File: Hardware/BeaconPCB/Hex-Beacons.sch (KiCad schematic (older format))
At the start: 0 parts

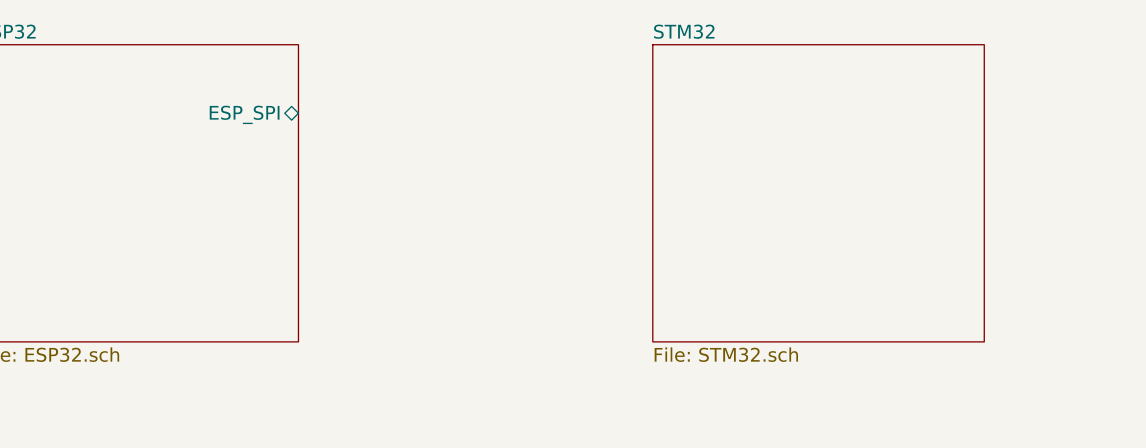
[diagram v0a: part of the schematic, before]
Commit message: Base STM32 circuit schematic done
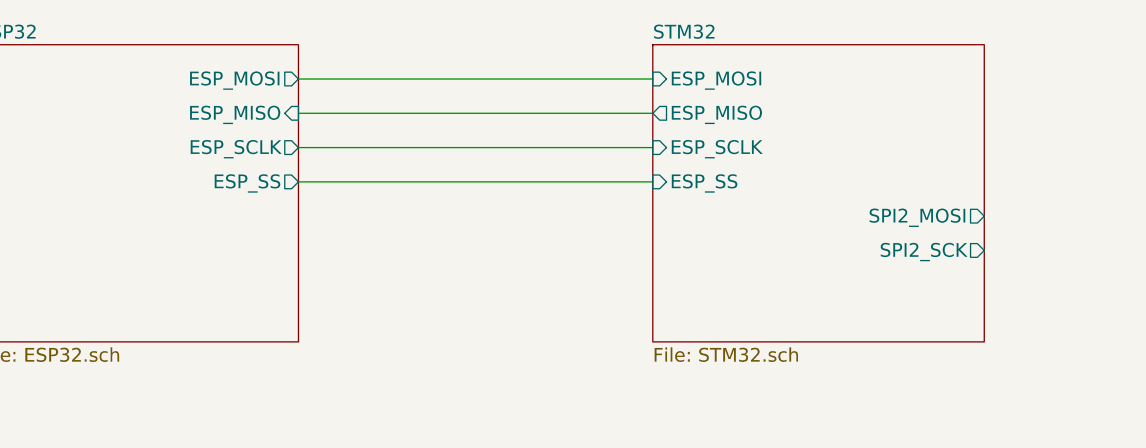
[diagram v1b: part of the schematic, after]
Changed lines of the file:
@@
 F0 "ESP32" 60
 F1 "ESP32.sch" 60
-F2 "ESP_SPI" B R 4400 2600 60
+F2 "ESP_MOSI" O R 4400 2450 60
+F3 "ESP_MISO" I R 4400 2600 60
+F4 "ESP_SCLK" O R 4400 2750 60
+F5 "ESP_SS" O R 4400 2900 60
 $EndSheet
 $Sheet
@@
 F0 "STM32" 60
 F1 "STM32.sch" 60
+F2 "ESP_SS" I L 5950 2900 60
+F3 "ESP_SCLK" I L 5950 2750 60
+F4 "ESP_MISO" O L 5950 2600 60
+F5 "ESP_MOSI" I L 5950 2450 60
+F6 "SPI2_MOSI" O R 7400 3050 60
+F7 "SPI2_SCK" O R 7400 3200 60
 $EndSheet
 $Sheet
@@
 F1 "APA102.sch" 60
 $EndSheet
+Wire Wire Line
+	4400 2450 5950 2450
+Wire Wire Line
+	5950 2600 4400 2600
+Wire Wire Line
+	4400 2750 5950 2750
+Wire Wire Line
+	5950 2900 4400 2900
 $EndSCHEMATC

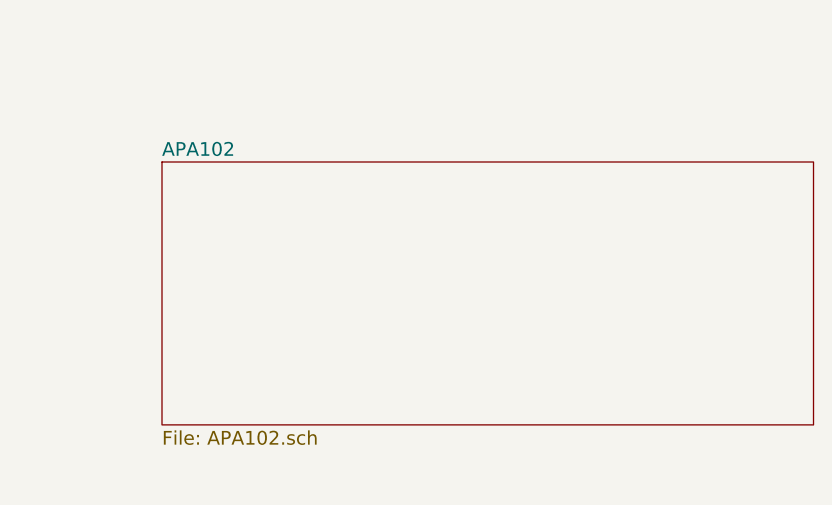
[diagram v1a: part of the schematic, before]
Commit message: Added IO buffers and APA102
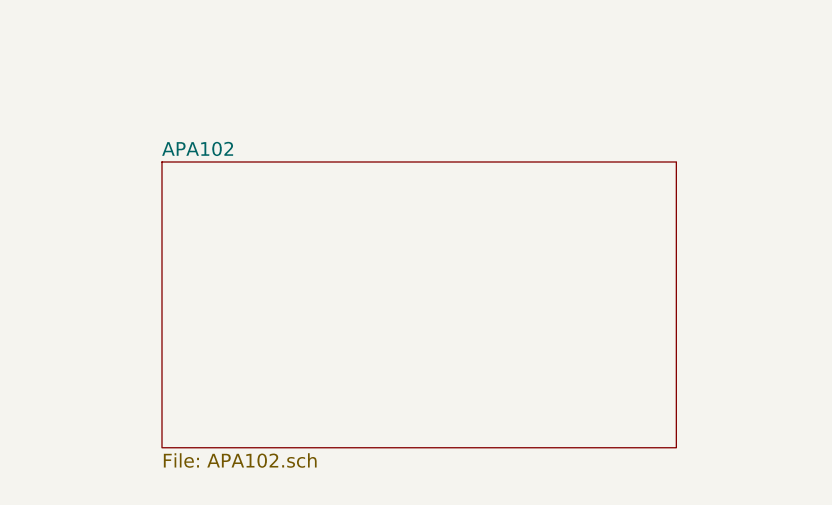
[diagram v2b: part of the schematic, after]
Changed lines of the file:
@@
 LIBS:valves
 LIBS:STM32F042C6T6
+LIBS:crumpschemes
 LIBS:Hex-Beacons-cache
 EELAYER 25 0
@@
 $EndSheet
 $Sheet
-S 7000 4650 2850 1150
+S 7000 4650 2250 1250
 U 59ADAAF7
 F0 "APA102" 60

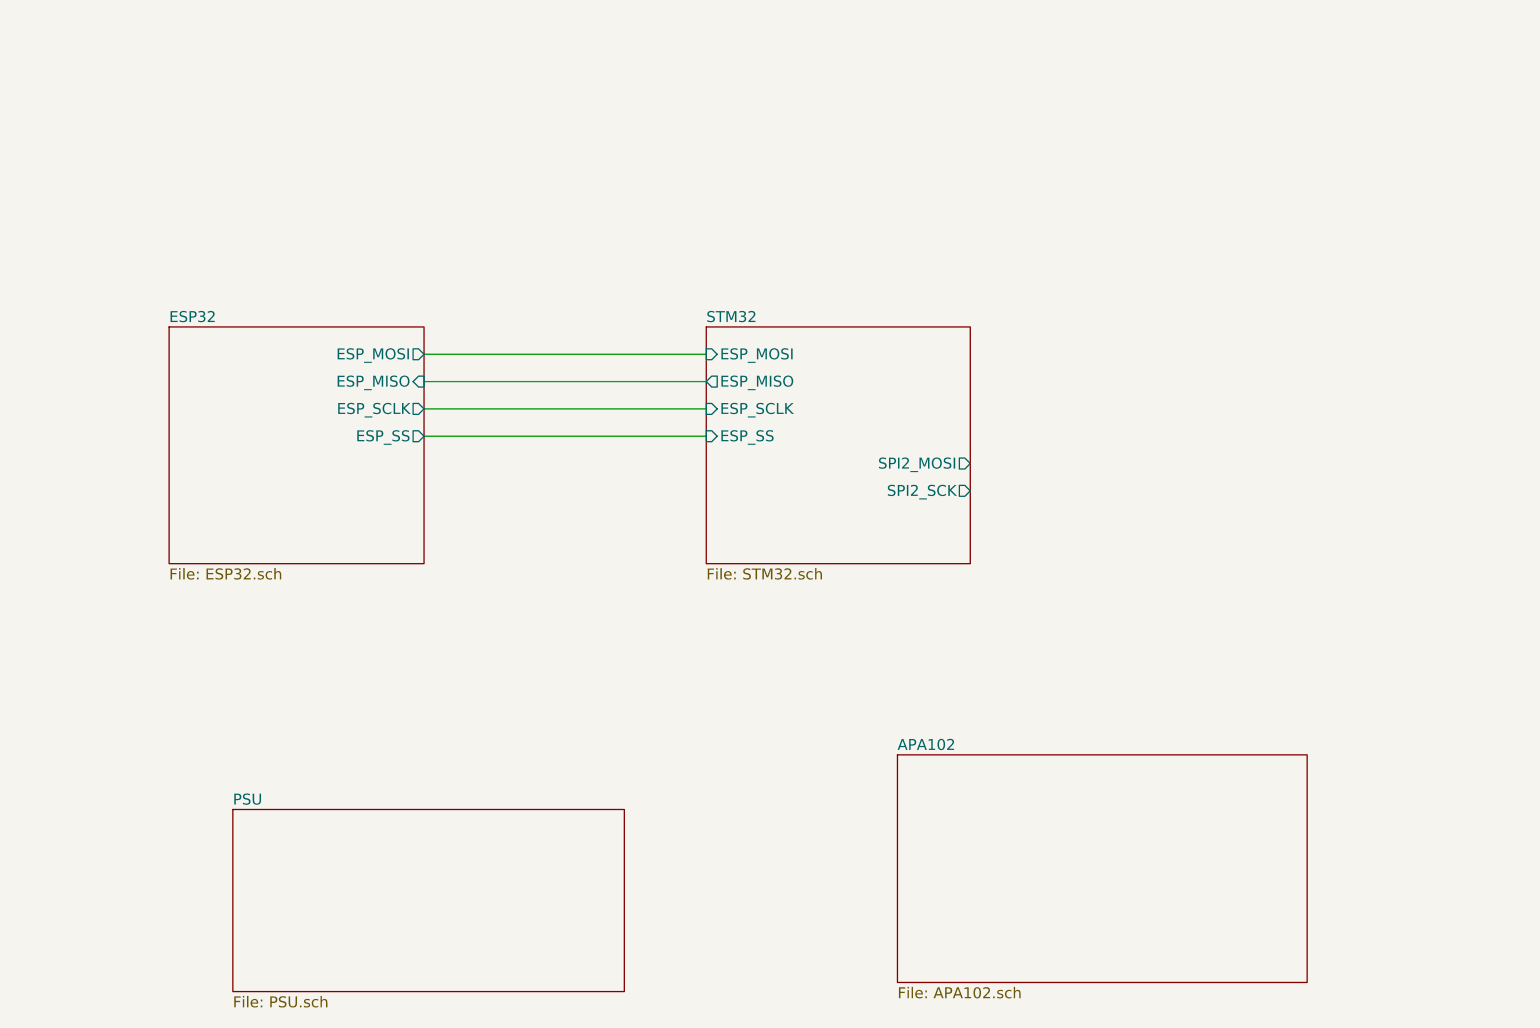
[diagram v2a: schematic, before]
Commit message: Added Connectors Sheet
Started to re-arrange SPI lines
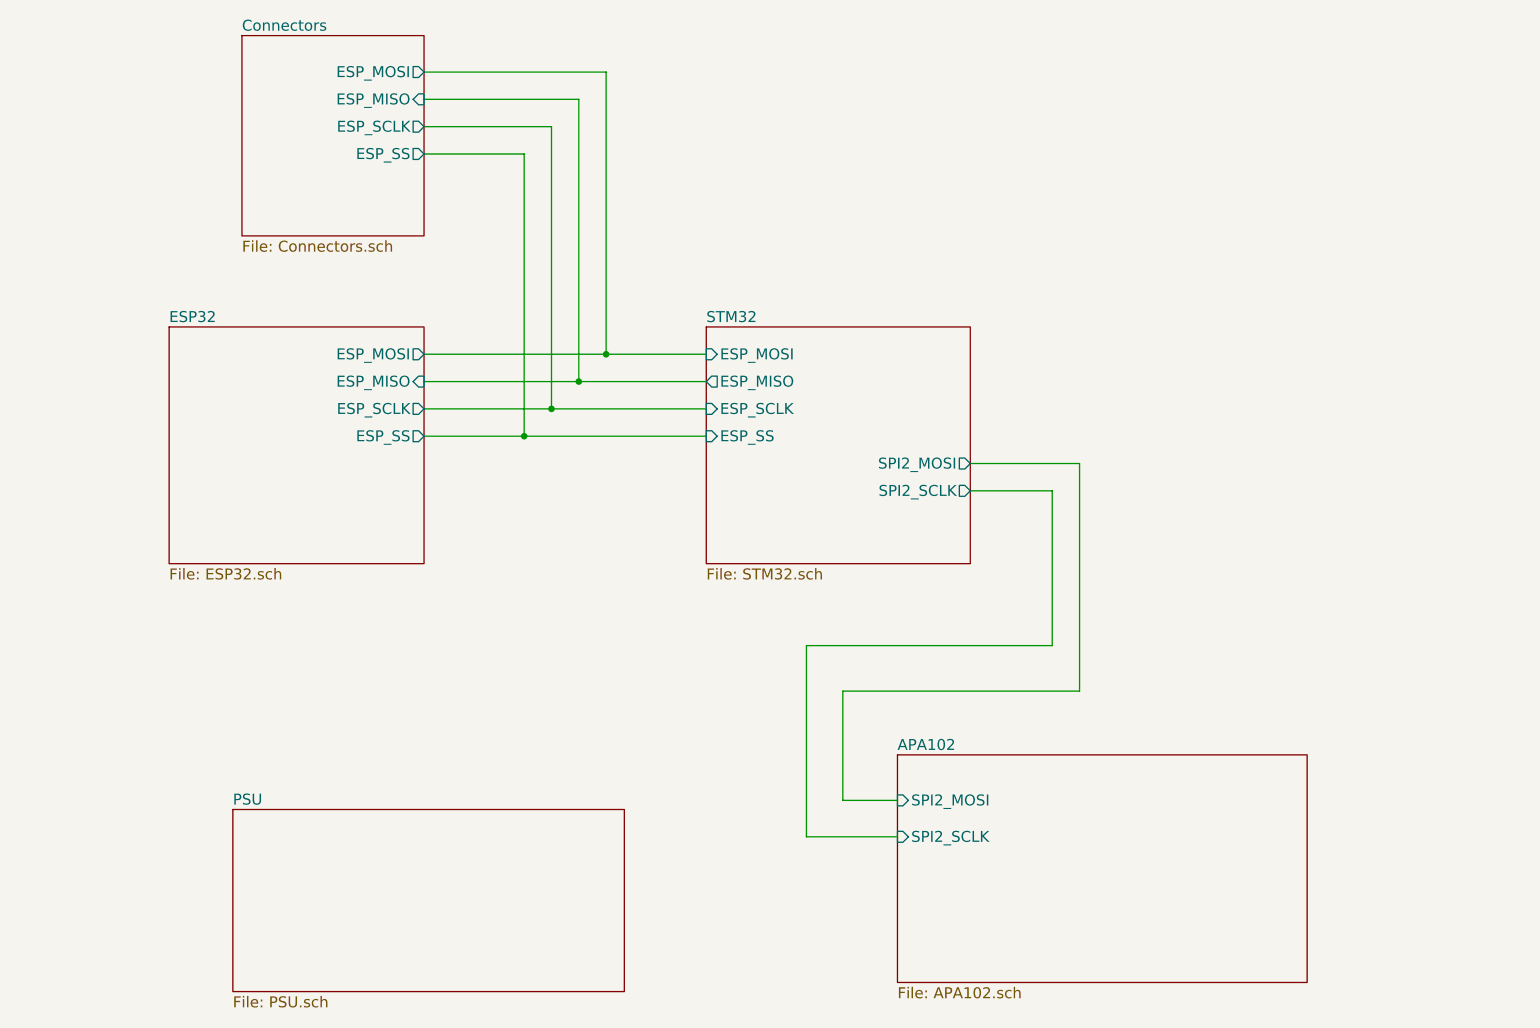
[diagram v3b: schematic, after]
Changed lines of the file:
@@
 $Descr A4 11693 8268
 encoding utf-8
-Sheet 1 5
+Sheet 1 6
 Title ""
 Date ""
@@
 F5 "ESP_MOSI" I L 5950 2450 60
 F6 "SPI2_MOSI" O R 7400 3050 60
-F7 "SPI2_SCK" O R 7400 3200 60
+F7 "SPI2_SCLK" O R 7400 3200 60
 $EndSheet
 $Sheet
@@
 F0 "APA102" 60
 F1 "APA102.sch" 60
+F2 "SPI2_MOSI" I L 7000 4900 60
+F3 "SPI2_SCLK" I L 7000 5100 60
 $EndSheet
 Wire Wire Line
-	4400 2450 5950 2450
+	4400 2450 5400 2450
 Wire Wire Line
-	5950 2600 4400 2600
+	5400 2450 5950 2450
 Wire Wire Line
-	4400 2750 5950 2750
+	5950 2600 5250 2600
 Wire Wire Line
-	5950 2900 4400 2900
+	5250 2600 4400 2600
+Wire Wire Line
+	4400 2750 5100 2750
+Wire Wire Line
+	5100 2750 5950 2750
+Wire Wire Line
+	5950 2900 4950 2900
+Wire Wire Line
+	4950 2900 4400 2900
+$Sheet
+S 3400 700  1000 1100
+U 59B35FE0
+F0 "Connectors" 60
+F1 "Connectors.sch" 60
+F2 "ESP_MOSI" O R 4400 900 60
+F3 "ESP_MISO" I R 4400 1050 60
+F4 "ESP_SCLK" O R 4400 1200 60
+F5 "ESP_SS" O R 4400 1350 60
+$EndSheet
+Wire Wire Line
+	7000 5100 6500 5100
+Wire Wire Line
+	6500 5100 6500 4050
+Wire Wire Line
+	6500 4050 7850 4050
+Wire Wire Line
+	7850 4050 7850 3200
+Wire Wire Line
+	7850 3200 7400 3200
+Wire Wire Line
+	7400 3050 8000 3050
+Wire Wire Line
+	8000 3050 8000 4300
+Wire Wire Line
+	8000 4300 6700 4300
+Wire Wire Line
+	6700 4300 6700 4900
+Wire Wire Line
+	6700 4900 7000 4900
+Wire Wire Line
+	4400 1350 4950 1350
+Wire Wire Line
+	4950 1350 4950 2900
+Connection ~ 4950 2900
+Wire Wire Line
+	4400 1200 5100 1200
+Wire Wire Line
+	5100 1200 5100 2750
+Connection ~ 5100 2750
+Wire Wire Line
+	4400 1050 5250 1050
+Wire Wire Line
+	5250 1050 5250 2600
+Connection ~ 5250 2600
+Wire Wire Line
+	4400 900  5400 900
+Wire Wire Line
+	5400 900  5400 2450
+Connection ~ 5400 2450
 $EndSCHEMATC

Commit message: Minor schematic adjustments
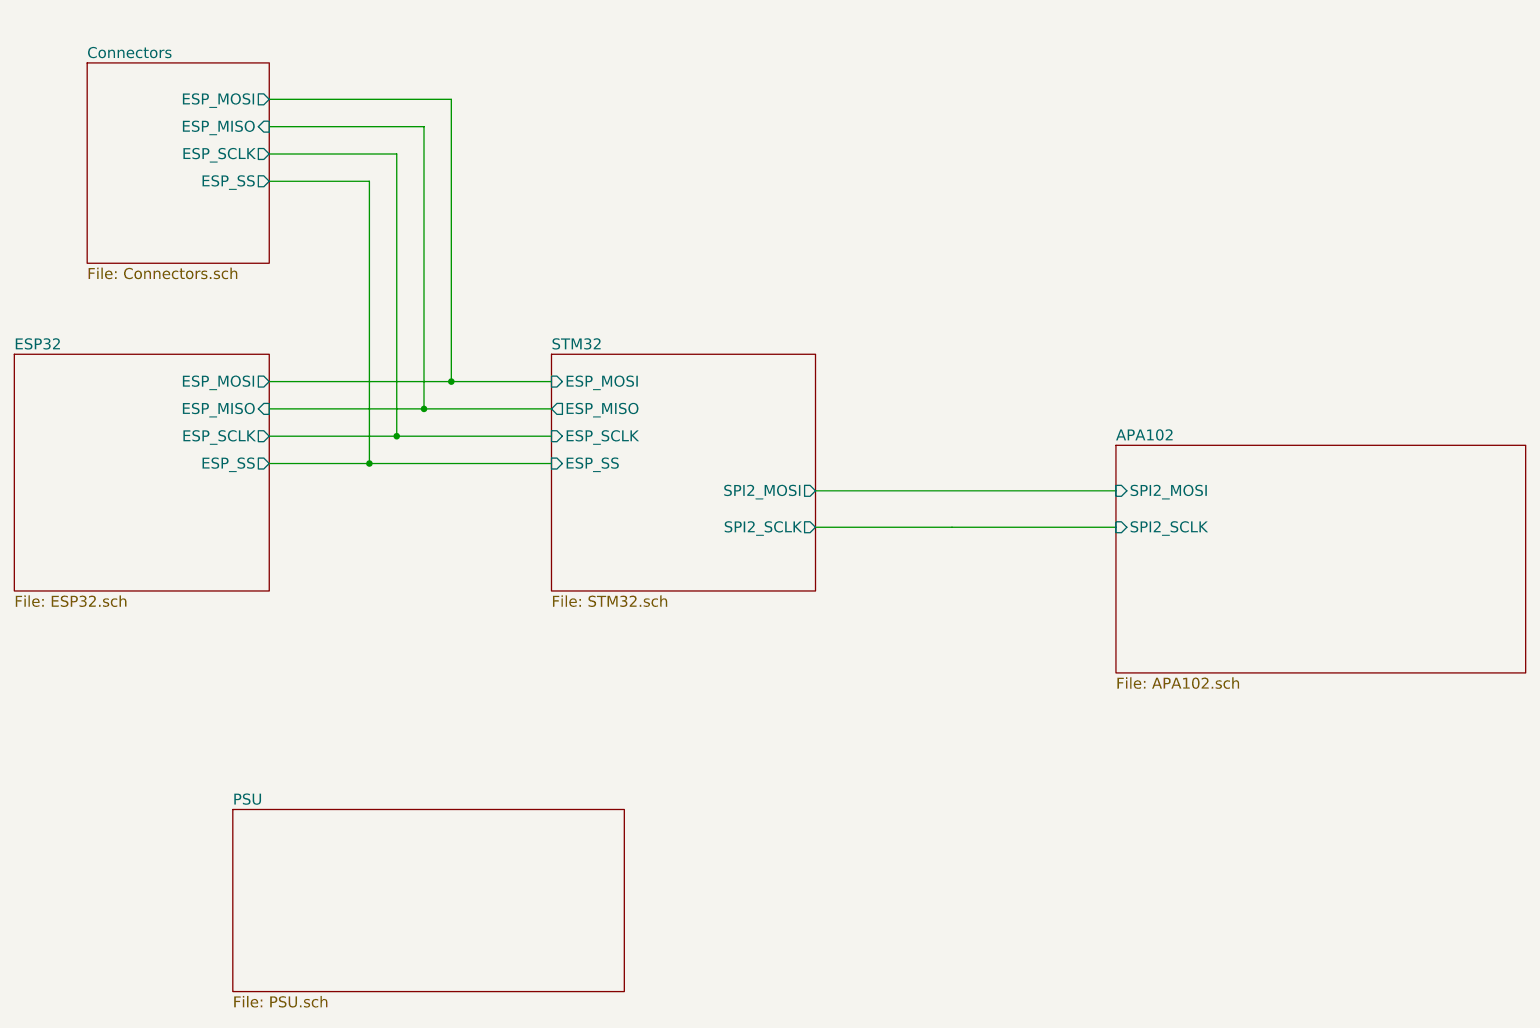
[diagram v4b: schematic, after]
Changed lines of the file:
@@
 $EndDescr
 $Sheet
-S 3000 2300 1400 1300
+S 2150 2450 1400 1300
 U 59AC571E
 F0 "ESP32" 60
 F1 "ESP32.sch" 60
-F2 "ESP_MOSI" O R 4400 2450 60
-F3 "ESP_MISO" I R 4400 2600 60
-F4 "ESP_SCLK" O R 4400 2750 60
-F5 "ESP_SS" O R 4400 2900 60
+F2 "ESP_MOSI" O R 3550 2600 60
+F3 "ESP_MISO" I R 3550 2750 60
+F4 "ESP_SCLK" O R 3550 2900 60
+F5 "ESP_SS" O R 3550 3050 60
 $EndSheet
 $Sheet
-S 5950 2300 1450 1300
+S 5100 2450 1450 1300
 U 59AC5A80
 F0 "STM32" 60
 F1 "STM32.sch" 60
-F2 "ESP_SS" I L 5950 2900 60
-F3 "ESP_SCLK" I L 5950 2750 60
-F4 "ESP_MISO" O L 5950 2600 60
-F5 "ESP_MOSI" I L 5950 2450 60
-F6 "SPI2_MOSI" O R 7400 3050 60
-F7 "SPI2_SCLK" O R 7400 3200 60
+F2 "ESP_SS" I L 5100 3050 60
+F3 "ESP_SCLK" I L 5100 2900 60
+F4 "ESP_MISO" O L 5100 2750 60
+F5 "ESP_MOSI" I L 5100 2600 60
+F6 "SPI2_MOSI" O R 6550 3200 60
+F7 "SPI2_SCLK" O R 6550 3400 60
 $EndSheet
 $Sheet
@@
 $EndSheet
 $Sheet
-S 7000 4650 2250 1250
+S 8200 2950 2250 1250
 U 59ADAAF7
 F0 "APA102" 60
 F1 "APA102.sch" 60
-F2 "SPI2_MOSI" I L 7000 4900 60
-F3 "SPI2_SCLK" I L 7000 5100 60
+F2 "SPI2_MOSI" I L 8200 3200 60
+F3 "SPI2_SCLK" I L 8200 3400 60
 $EndSheet
 Wire Wire Line
-	4400 2450 5400 2450
+	3550 2600 4550 2600
 Wire Wire Line
-	5400 2450 5950 2450
+	4550 2600 5100 2600
 Wire Wire Line
-	5950 2600 5250 2600
-Wire Wire Line
-	5250 2600 4400 2600
+	3550 2750 4400 2750
 Wire Wire Line
 	4400 2750 5100 2750
 Wire Wire Line
-	5100 2750 5950 2750
+	3550 2900 4250 2900
 Wire Wire Line
-	5950 2900 4950 2900
+	4250 2900 5100 2900
 Wire Wire Line
-	4950 2900 4400 2900
+	3550 3050 4100 3050
+Wire Wire Line
+	4100 3050 5100 3050
 $Sheet
-S 3400 700  1000 1100
+S 2550 850  1000 1100
 U 59B35FE0
 F0 "Connectors" 60
 F1 "Connectors.sch" 60
-F2 "ESP_MOSI" O R 4400 900 60
-F3 "ESP_MISO" I R 4400 1050 60
-F4 "ESP_SCLK" O R 4400 1200 60
-F5 "ESP_SS" O R 4400 1350 60
+F2 "ESP_MOSI" O R 3550 1050 60
+F3 "ESP_MISO" I R 3550 1200 60
+F4 "ESP_SCLK" O R 3550 1350 60
+F5 "ESP_SS" O R 3550 1500 60
 $EndSheet
 Wire Wire Line
-	7000 5100 6500 5100
+	6550 3400 7300 3400
 Wire Wire Line
-	6500 5100 6500 4050
+	6550 3200 8200 3200
 Wire Wire Line
-	6500 4050 7850 4050
+	3550 1500 4100 1500
 Wire Wire Line
-	7850 4050 7850 3200
+	4100 1500 4100 3050
+Connection ~ 4100 3050
 Wire Wire Line
-	7850 3200 7400 3200
+	3550 1350 4250 1350
 Wire Wire Line
-	7400 3050 8000 3050
+	4250 1350 4250 2900
+Connection ~ 4250 2900
 Wire Wire Line
-	8000 3050 8000 4300
+	3550 1200 4400 1200
 Wire Wire Line
-	8000 4300 6700 4300
+	4400 1200 4400 2750
+Connection ~ 4400 2750
 Wire Wire Line
-	6700 4300 6700 4900
+	3550 1050 4550 1050
 Wire Wire Line
-	6700 4900 7000 4900
+	4550 1050 4550 2600
+Connection ~ 4550 2600
 Wire Wire Line
-	4400 1350 4950 1350
+	7300 3400 7300 3400
 Wire Wire Line
-	4950 1350 4950 2900
-Connection ~ 4950 2900
-Wire Wire Line
-	4400 1200 5100 1200
-Wire Wire Line
-	5100 1200 5100 2750
-Connection ~ 5100 2750
-Wire Wire Line
-	4400 1050 5250 1050
-Wire Wire Line
-	5250 1050 5250 2600
-Connection ~ 5250 2600
-Wire Wire Line
-	4400 900  5400 900
-Wire Wire Line
-	5400 900  5400 2450
-Connection ~ 5400 2450
+	7300 3400 8200 3400
 $EndSCHEMATC
